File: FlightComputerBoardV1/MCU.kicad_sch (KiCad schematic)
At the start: 0 parts

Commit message: Added power supply for MCU sheet
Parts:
- added U20: STM32H723ZGTx, Package_QFP:LQFP-144_20x20mm_P0.5mm, symbol MCU_ST_STM32H7:STM32H723ZGTx
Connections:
- new net: U20.107 (VSS), U20.120 (VSS), U20.130 (VSS), U20.16 (VSS), U20.38 (VSS), U20.51 (VSS), U20.61 (VSS), U20.83 (VSS), U20.94 (VSS)
- new net +3V3: U20.108 (VDD), U20.121 (VDD), U20.131 (VDD), U20.144 (VDD), U20.17 (VDD), U20.30 (VDD), U20.33 (VDDA), U20.39 (VDD), U20.52 (VDD), U20.6 (VBAT), U20.62 (VDD), U20.72 (VDD), U20.84 (VDD), U20.95 (VDD33USB)
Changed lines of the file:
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@@
 	(generator "eeschema")
 	(generator_version "10.0")
-	(paper "A4")
-)
+	(paper "A3")

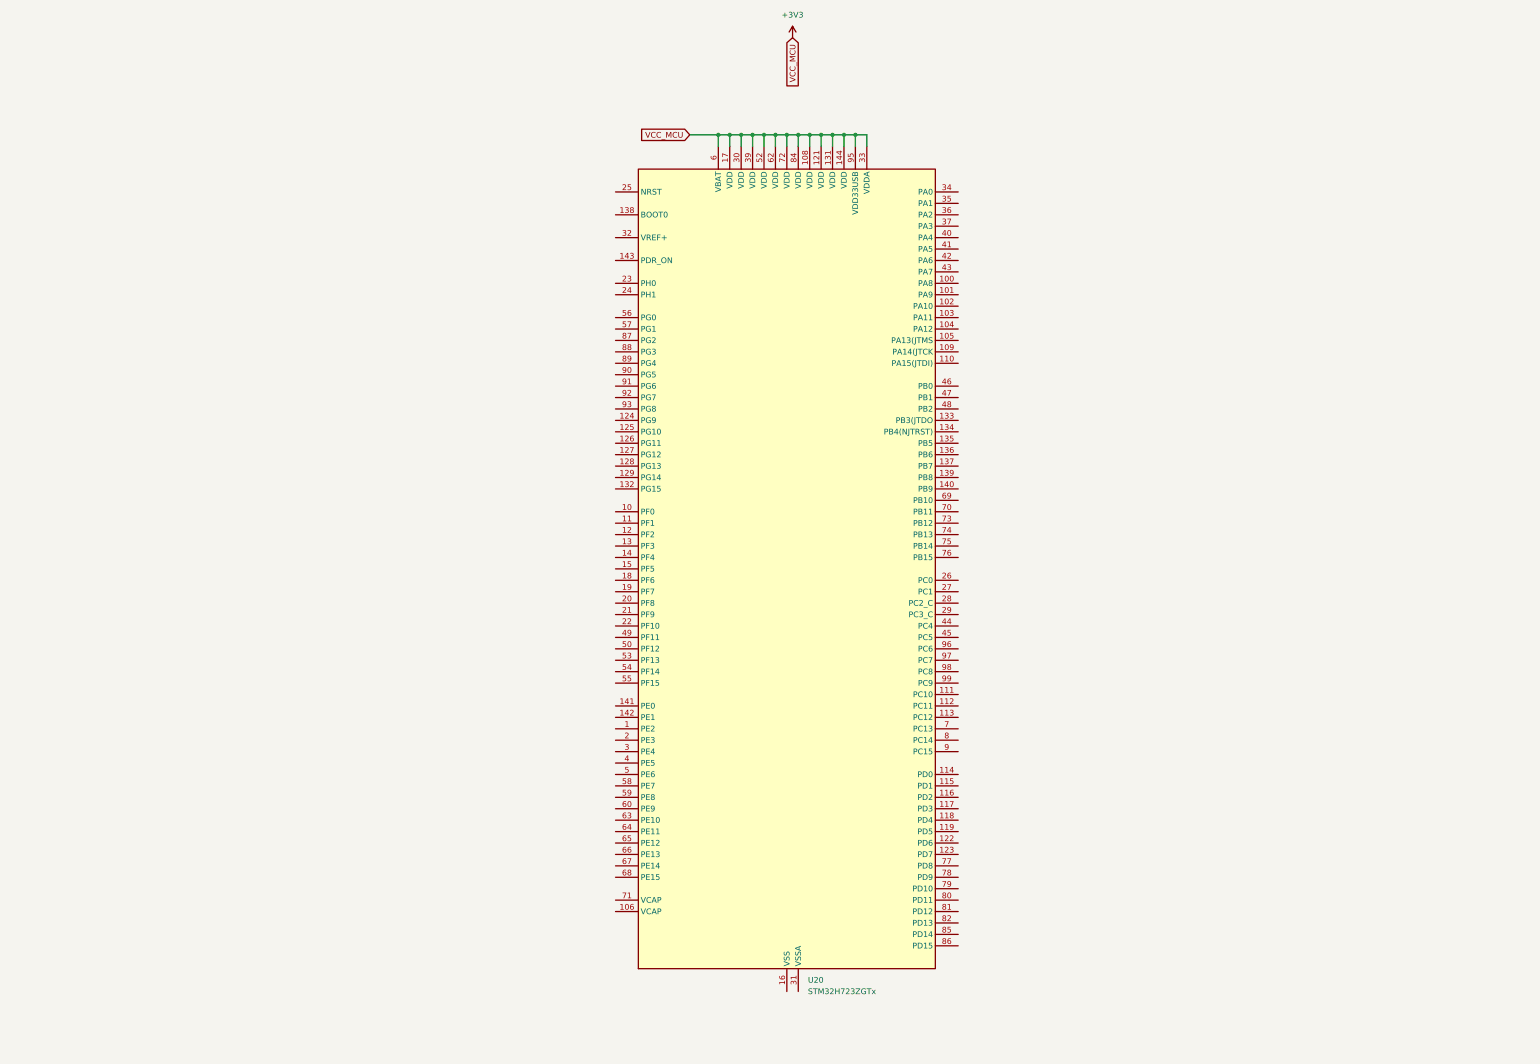
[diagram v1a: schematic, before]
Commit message: Finished Power section of the MCU sheet
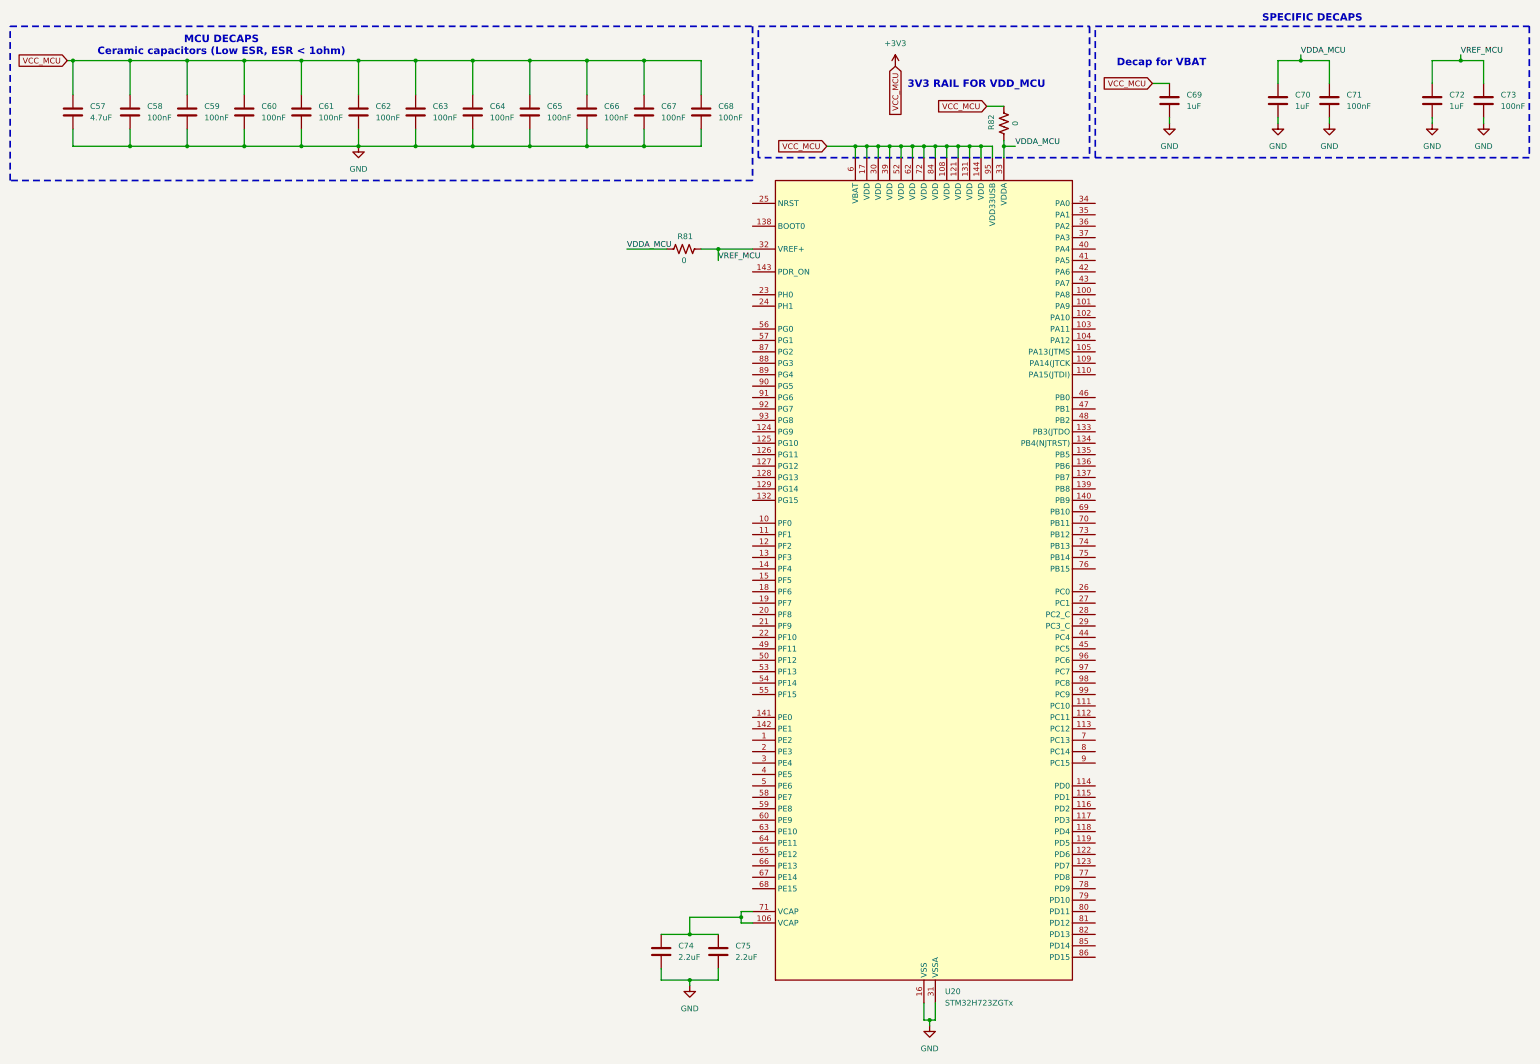
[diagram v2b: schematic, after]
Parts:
- added C57: 4.7uF, symbol Device:C
- added C58, C59, C60, C61, C62, C63, C64, C65, C66, C67, C68, C71, C73: 100nF, symbol Device:C
- added C69, C70, C72: 1uF, symbol Device:C
- added C74, C75: 2.2uF, symbol Device:C
- added R81, R82: 0, Converter_DCDC:Converter_DCDC_RECOM_R-78B-2.0_THT, symbol Device:R_US
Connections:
- net +3V3: now also C57.1, C58.1, C59.1, C60.1, C61.1, C62.1, C63.1, C64.1, C65.1, C66.1, C67.1, C68.1, C69.1, R82.2; no longer U20.33 (VDDA)
- net at U20.106 (VCAP): now also U20.71 (VCAP), C74.1, C75.1
- net GND: now reaches U20.107 (VSS), U20.120 (VSS), U20.130 (VSS), U20.16 (VSS), U20.38 (VSS), U20.51 (VSS), U20.61 (VSS), U20.83 (VSS), U20.94 (VSS)
- net GND: now also U20.31 (VSSA), C57.2, C58.2, C59.2, C60.2, C61.2, C62.2, C63.2, C64.2, C65.2, C66.2, C67.2, C68.2, C69.2, C70.2, C71.2, C72.2, C73.2, C74.2, C75.2
- net VREF_MCU: now reaches U20.32 (VREF+)
- net VREF_MCU: now also C72.1, C73.1, R81.2
- new net VDDA_MCU: C70.1, C71.1, R81.1, R82.1, U20.33 (VDDA)
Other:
- note added: "3V3 RAIL FOR VDD_MCU"
- note added: "Decap for VBAT"
- note added: "MCU DECAPS Ceramic capacitors (Low ESR, ESR < 1ohm)"
- note added: "SPECIFIC DECAPS"
- moved on the sheet: U20
